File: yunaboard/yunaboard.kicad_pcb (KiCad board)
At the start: 4 copper layers, 40 x 25 mm, 49 parts, among them J1 USB-C Receptacle USB 2.0, J2 JTAG/SWD Tag Connect, J3 PCB ANT, J4 GPIO Header 1, J5 GPIO Header 2, U1 ESP32-S3, U2 CP2102N-Axx-xQFN28, U3 USBLC6-2SC6, U4 MIC5365-3.3YD5, Y1 40 MHz (±10ppm)

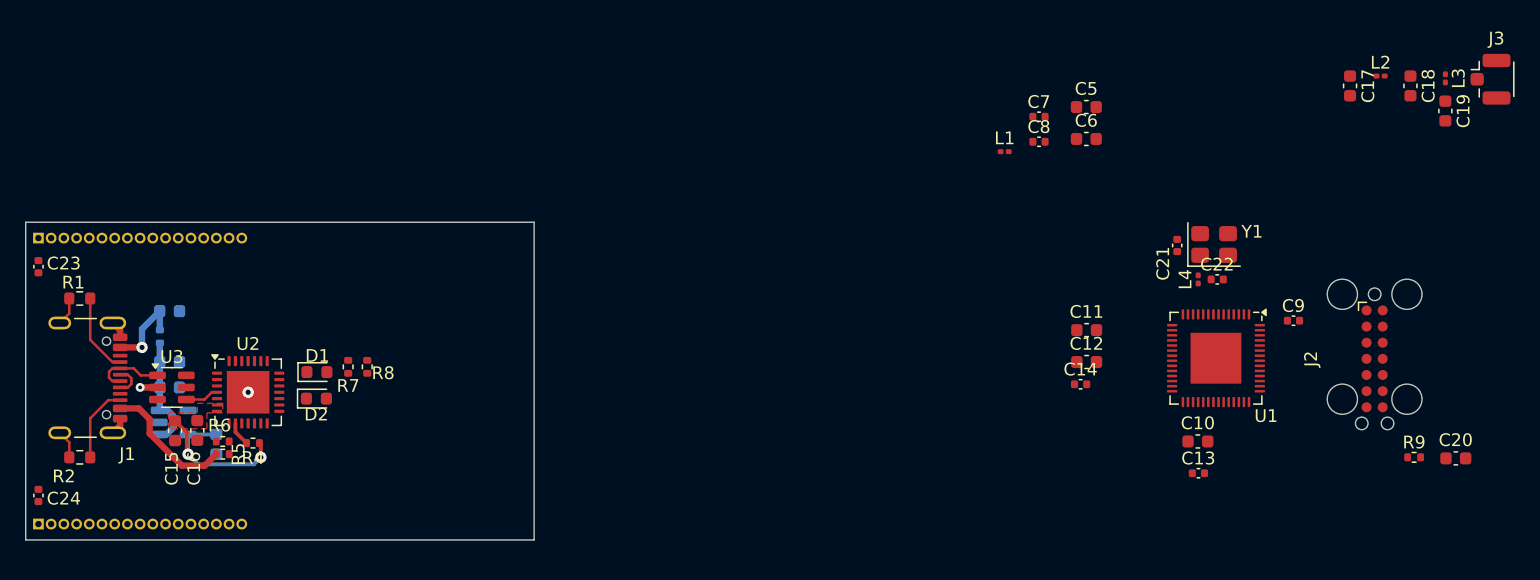
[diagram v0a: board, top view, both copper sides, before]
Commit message: Update
- Changed JTAG connector to pin header for SWD
- Changed GPIO pin headers from 1mm length to 2mm length
- Adjusted the layout of the PCB from the initial design
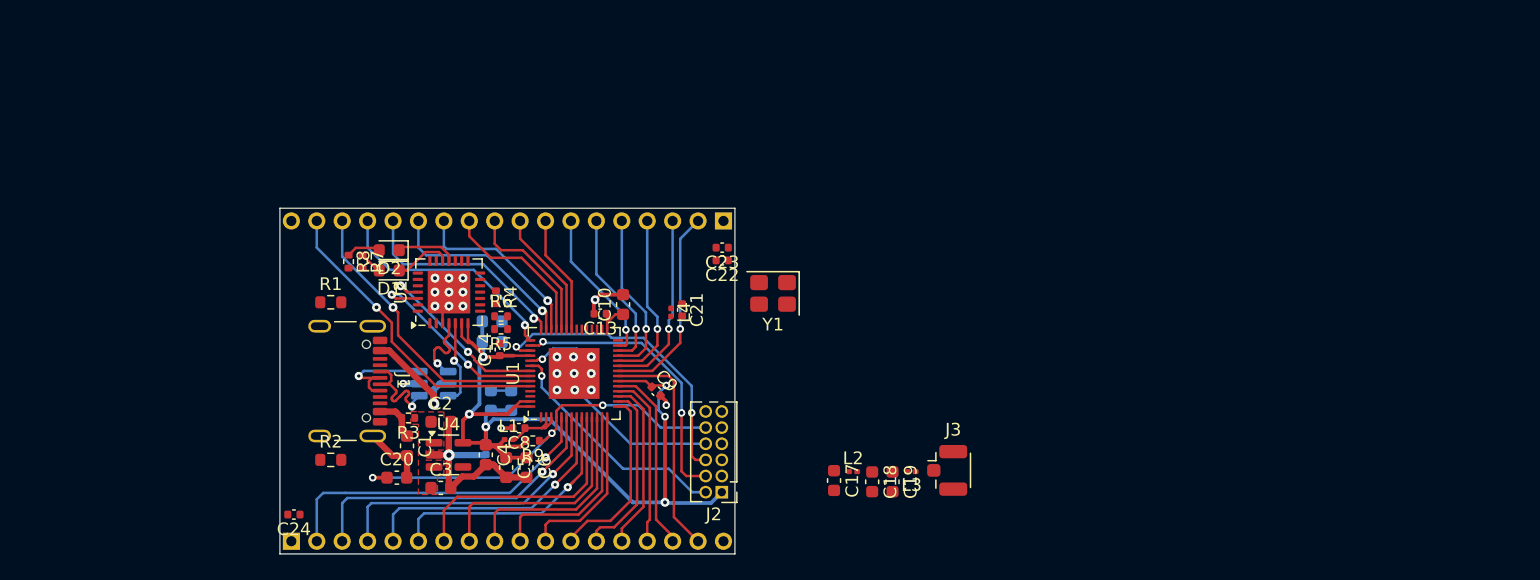
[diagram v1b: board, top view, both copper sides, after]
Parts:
- removed J5: GPIO Header 2, Connector_PinHeader_1.00mm:PinHeader_1x17_P1.00mm_Vertical
- added J6: GPIO Header 1, Connector_PinHeader_2.00mm:PinHeader_1x18_P2.00mm_Vertical, B.Cu at (95.9, 110.1)
- C1, C2, C3, C4, R3, U4: moved to F.Cu
- C11, C12, C15, C16, C7, U3: moved to B.Cu
- J2: value JTAG/SWD Tag Connect -> JTAG/SWD Header; footprint Connector:Tag-Connect_TC2070-IDC-FP_2x07_P1.27mm_Vertical -> Connector_PinHeader_1.27mm:PinHeader_2x06_P1.27mm_Vertical
- J4: value GPIO Header 1 -> GPIO Header 2; footprint Connector_PinHeader_1.00mm:PinHeader_1x17_P1.00mm_Vertical -> Connector_PinHeader_2.00mm:PinHeader_1x18_P2.00mm_Vertical
- moved C20 83.3 mm to (104.2, 105.1)
- moved R9 69.4 mm to (114.9, 102.2), turned to 180 degrees
- moved J4 58.9 mm to (129.9, 84.9), turned to 90 degrees
- moved C23 53.8 mm to (129.8, 87.0), turned to 180 degrees
- moved C5 53.7 mm to (112.8, 104.3), turned to -90 degrees
- moved J3 52.7 mm to (147.5, 104.5)
- moved C18 52.6 mm to (141.6, 105.4)
- moved J2 52.4 mm to (129.8, 106.2), turned to 180 degrees
- moved C19 52.4 mm to (143.2, 105.4)
- moved L3 52.2 mm to (144.7, 104.6), turned to 180 degrees
- moved L2 51.9 mm to (140.1, 104.6)
- moved C17 51.1 mm to (138.6, 105.3)
- moved C6 51.1 mm to (114.4, 104.3), turned to -90 degrees
- moved C7 50.8 mm to (111.2, 102.8), turned to -90 degrees
- moved U1 50.5 mm to (118.2, 96.9), turned to 90 degrees
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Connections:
- C24 pad 1: +VBUSF -> +VBUS
- J4 pad 1: +VBUSF -> +3V3
- J4 pad 10: /GPIO8 -> /GPIO33
- J4 pad 11: /GPIO9 -> /GPIO34
- J4 pad 12: /GPIO10 -> /GPIO35
- J4 pad 13: /GPIO11 -> /GPIO36
- J4 pad 14: /GPIO12 -> /GPIO37
- J4 pad 15: /GPIO13 -> /GPIO38
- J4 pad 16: /GPIO14 -> /GPIO45
- J4 pad 17: GND -> /GPIO46
- J4 pad 2: /GPIO0/ADC_CH0 -> /GPIO16
- J4 pad 3: /GPIO1/ADC_CH1 -> /GPIO17
- J4 pad 4: /GPIO2/ADC_CH2 -> /GPIO18
- J4 pad 5: /GPIO3/ADC_CH3 -> /GPIO19
- J4 pad 6: /GPIO4/I2C_SCL0 -> /GPIO20
- J4 pad 7: /GPIO5/I2C_SDA0 -> /GPIO21
- J4 pad 8: /GPIO6/I2C_SCL1 -> /GPIO31
- J4 pad 9: /GPIO7/I2C_SDA1 -> /GPIO32
- U1 pad 51: /GPIO20 -> /GPIO45
- U1 pad 52: /GPIO21 -> /GPIO46
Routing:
- net +3V3: track 14.3 -> 77.5 mm, vias 2 -> 6
- net /CHIP_PU: track 0.00 -> 32.5 mm, vias 0 -> 3
- net /GPIO0/ADC_CH0: track 0.00 -> 26.3 mm, vias 0 -> 1
- net /GPIO1/ADC_CH1: track 0.00 -> 24.9 mm, vias 0 -> 1
- net /GPIO46: track 0.00 -> 24.3 mm, vias 0 -> 1
- net /TDO: track 0.00 -> 23.9 mm, vias 0 -> 2
- net /GPIO2/ADC_CH2: track 0.00 -> 23.4 mm, vias 0 -> 1
- net GND: track 8.56 -> 31.6 mm, vias 2 -> 23
- net /GPIO45: track 0.00 -> 22.7 mm, vias 0 -> 1
- net /TCK: track 0.00 -> 22.4 mm, vias 0 -> 2
- net /GPIO3/ADC_CH3: track 0.00 -> 21.8 mm, vias 0 -> 1
- net /GPIO4/I2C_SCL0: track 0.00 -> 21.2 mm, vias 0 -> 1
- net /GPIO5/I2C_SDA0: track 0.00 -> 19.8 mm
- net /TDI: track 0.00 -> 19.2 mm, vias 0 -> 1
- net /TMS: track 0.00 -> 18.8 mm, vias 0 -> 1
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- added copper zone on F.Cu, net +VBUSF
- removed copper zone on F.Cu, net +3V3
- removed copper zone on In1.Cu, net GND
- removed copper zone on In2.Cu, net GND
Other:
- board size 40 x 25 mm -> 35.8 x 27.2 mm
- copper layers 4 -> 2

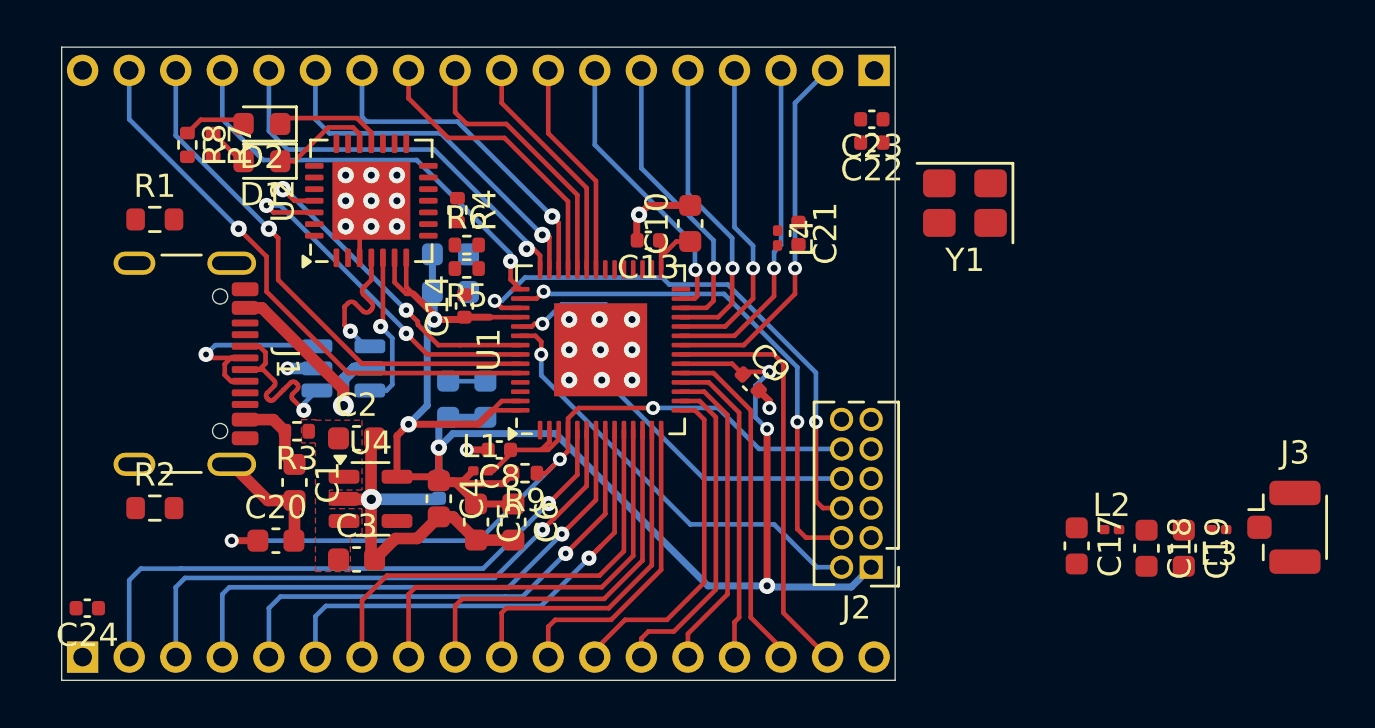
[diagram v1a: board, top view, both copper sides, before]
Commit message: Finalzed PCB
- Changed LDO to TLV75533PDBVR for an output current of 500 mA
- Adjusted some  routing to reduce ground plane breaking
- Adjusted some 3V3 traces to be 0.5mm instead of 0.3mm
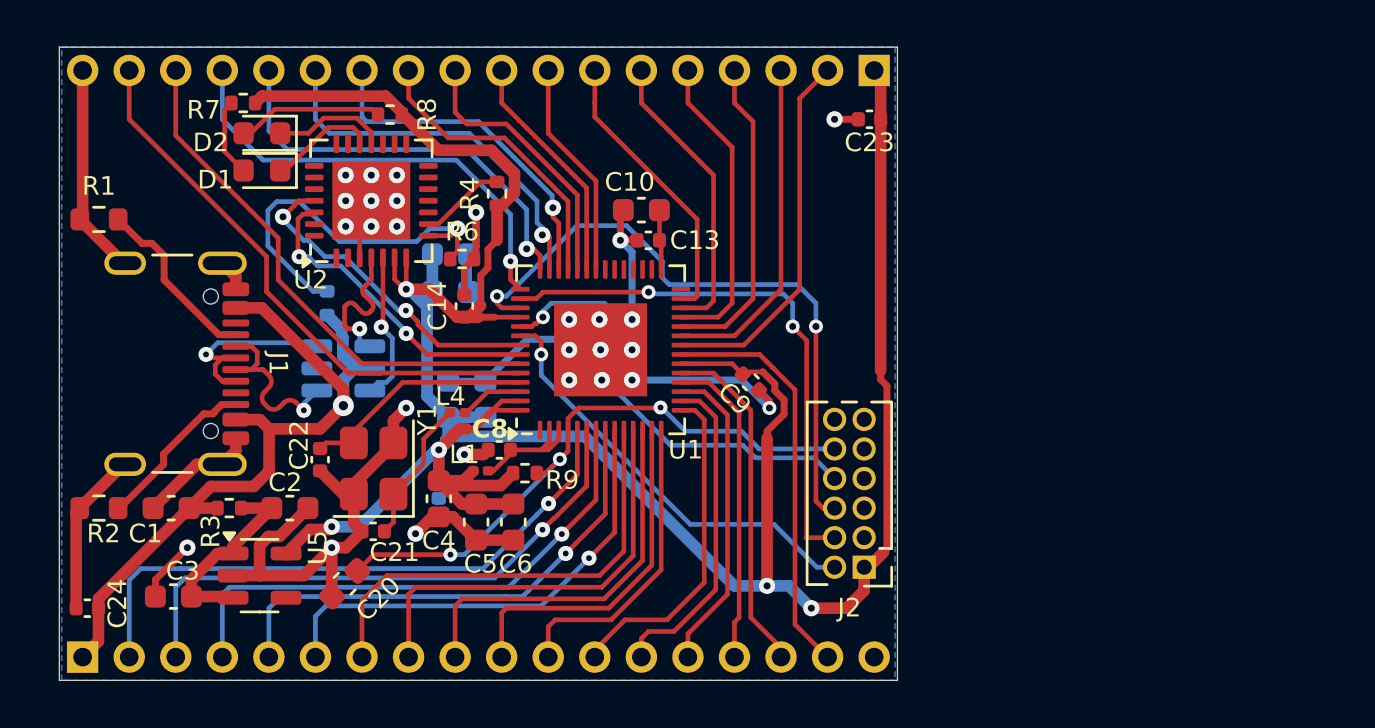
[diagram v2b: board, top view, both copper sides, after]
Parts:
- removed C17, C18, C19: 10u, Capacitor_SMD:C_0603_1608Metric
- removed J3: PCB ANT, Connector_Coaxial:U.FL_Hirose_U.FL-R-SMT-1_Vertical
- removed L2, L3: 2.0n, Inductor_SMD:L_0201_0603Metric
- removed U4: MIC5365-3.3YD5, Package_TO_SOT_SMD:TSOT-23-5
- added U5: TLV75533PDBV, Package_TO_SOT_SMD:SOT-23-5, F.Cu at (103.5, 106.6)
- R5: moved to B.Cu
- moved Y1 27.8 mm to (108.4, 102.0), turned to 90 degrees
- moved C22 27.3 mm to (106.1, 101.6), turned to -90 degrees
- moved C21 22.3 mm to (108.4, 104.7), turned to 180 degrees
- moved L4 15.7 mm to (112.0, 99.6), turned to 0 degrees
- moved R8 8.80 mm to (109.1, 86.8), turned to 0 degrees
- moved C3 8.03 mm to (99.8, 107.5), turned to 180 degrees
- moved R5 6.18 mm to (106.4, 94.9), turned to 90 degrees
- moved C1 5.41 mm to (99.7, 103.7), turned to 180 degrees
- moved R3 4.39 mm to (102.2, 103.7)
- moved C2 4.14 mm to (104.8, 103.7)
- moved C20 3.48 mm to (107.2, 106.9), turned to -135 degrees
- moved R1 2.40 mm to (96.6, 91.3)
- moved R2 2.40 mm to (96.6, 103.7)
- moved R7 2.22 mm to (102.8, 86.3), turned to 0 degrees
- moved C10 2.18 mm to (119.9, 90.9), turned to 180 degrees
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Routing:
- net GND: track 31.6 -> 83.1 mm, vias 23 -> 27
- net +3V3: track 77.5 -> 125.2 mm, vias 6 -> 5
- net +VBUS: track 12.3 -> 32.9 mm
- net Net-(U2-VBUS): track 0.00 -> 16.9 mm, vias 0 -> 1
- net /XTAL_N: track 0.00 -> 10.1 mm
- net +VBUSF: track 0.00 -> 9.02 mm
- net Net-(J1-CC1): track 0.00 -> 7.72 mm
- net Net-(J1-CC2): track 0.00 -> 7.58 mm
- net /CHIP_PU: track 32.5 -> 26.2 mm
- net Net-(C21-Pad1): track 0.00 -> 6.27 mm
- net Net-(U2-~{RST}): track 0.00 -> 3.70 mm
- net /TDO: track 23.9 -> 27.5 mm
- net Net-(D2-A): track 2.72 -> 6.30 mm
- net /XTAL_P: track 0.00 -> 2.75 mm
- net /USB_TX: track 15.8 -> 13.8 mm
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- added copper zone on B.Cu, net GND
- removed copper zone on F.Cu, net +VBUSF
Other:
- board size 35.8 x 27.2 mm -> 36 x 27.2 mm
